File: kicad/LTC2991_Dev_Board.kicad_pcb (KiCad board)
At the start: 2 copper layers, 19.1 x 29.2 mm, 12 parts, among them P1 PIN_HEAD_1x8, P2 PIN_HEAD_1x8, P3 PIN_HEAD_2x3, P4 CONN_SENSE, Q1 MMBT3904, U1 LTC2991

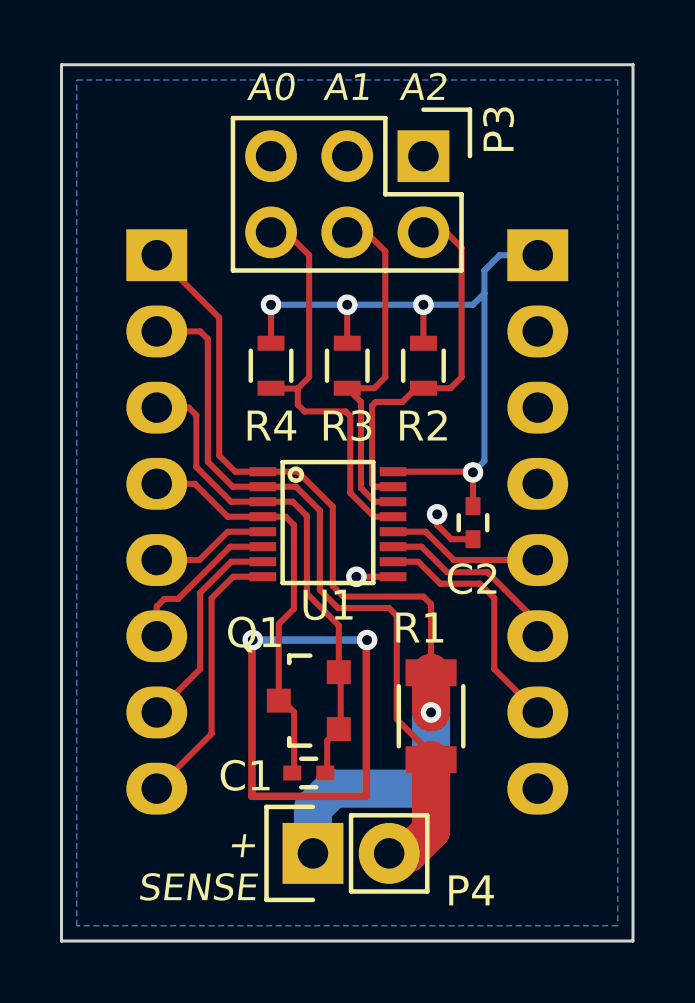
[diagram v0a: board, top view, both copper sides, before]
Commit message: Grounded Faraday traces surrounding temp-sensing transistor.
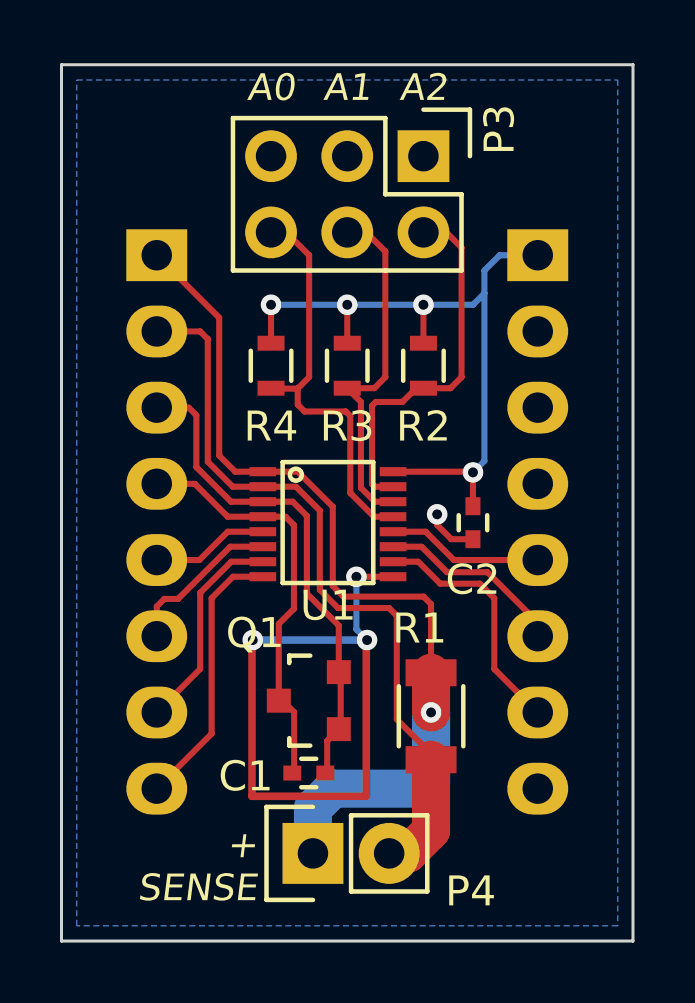
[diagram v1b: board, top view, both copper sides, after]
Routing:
- net /GND: track 2.98 -> 23.3 mm, vias 2 -> 4
- net (no net): track 18.0 -> 0.00 mm, vias 2 -> 0
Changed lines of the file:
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@@
     (thickness 1.6)
     (drawings 9)
-    (tracks 159)
+    (tracks 161)
     (zones 0)
     (modules 12)
@@
   (gr_line (start 150.495 117.221) (end 131.445 117.221) (angle 90) (layer Edge.Cuts) (width 0.1))
   (gr_line (start 131.445 88.011) (end 150.495 88.011) (angle 90) (layer Edge.Cuts) (width 0.1))
-  (segment (start 137.795 107.188) (end 137.795 112.395) (width 0.254) (layer F.Cu) (net 0))
-  (via (at 137.8204 107.188) (size 0.6858) (drill 0.3302) (layers F.Cu B.Cu) (net 0))
-  (segment (start 141.605 107.188) (end 137.795 107.188) (width 0.254) (layer B.Cu) (net 0))
-  (via (at 141.6304 107.188) (size 0.6858) (drill 0.3302) (layers F.Cu B.Cu) (net 0))
-  (segment (start 141.605 112.395) (end 141.605 107.188) (width 0.254) (layer F.Cu) (net 0))
-  (segment (start 137.795 112.395) (end 141.605 112.395) (width 0.254) (layer F.Cu) (net 0))
   (segment (start 145.161 102.7264) (end 145.161 101.6) (width 0.2032) (layer F.Cu) (net 1))
   (segment (start 142.4972 101.5764) (end 145.1374 101.5764) (width 0.2032) (layer F.Cu) (net 1))
@@
   (segment (start 139.2008 111.5568) (end 139.2008 109.59202) (width 0.2032) (layer F.Cu) (net 7))
   (segment (start 139.2008 109.59202) (end 138.75258 109.1438) (width 0.2032) (layer F.Cu) (net 7))
+  (segment (start 137.795 107.188) (end 137.795 112.395) (width 0.254) (layer F.Cu) (net 8))
+  (via (at 137.8204 107.188) (size 0.6858) (drill 0.3302) (layers F.Cu B.Cu) (net 8))
+  (segment (start 141.605 107.188) (end 137.795 107.188) (width 0.254) (layer B.Cu) (net 8))
+  (via (at 141.6304 107.188) (size 0.6858) (drill 0.3302) (layers F.Cu B.Cu) (net 8) (status 80))
+  (segment (start 141.2782 105.0764) (end 141.2748 105.0798) (width 0.2032) (layer F.Cu) (net 8))
+  (via (at 141.2748 105.0798) (size 0.6858) (drill 0.3302) (layers F.Cu B.Cu) (net 8))
   (segment (start 142.4972 105.0764) (end 141.2782 105.0764) (width 0.2032) (layer F.Cu) (net 8))
-  (via (at 141.2748 105.0798) (size 0.6858) (drill 0.3302) (layers F.Cu B.Cu) (net 8))
-  (segment (start 141.2782 105.0764) (end 141.2748 105.0798) (width 0.2032) (layer F.Cu) (net 8))
+  (segment (start 141.2748 106.8324) (end 141.6304 107.188) (width 0.2032) (layer B.Cu) (net 8))
+  (segment (start 141.2748 105.0798) (end 141.2748 106.8324) (width 0.2032) (layer B.Cu) (net 8))
+  (segment (start 141.605 112.395) (end 141.605 107.188) (width 0.254) (layer F.Cu) (net 8))
+  (segment (start 137.795 112.395) (end 141.605 112.395) (width 0.254) (layer F.Cu) (net 8))
   (segment (start 145.161 103.8264) (end 144.441 103.8264) (width 0.2032) (layer F.Cu) (net 8))
   (via (at 143.9672 102.997) (size 0.6858) (drill 0.3302) (layers F.Cu B.Cu) (net 8))
